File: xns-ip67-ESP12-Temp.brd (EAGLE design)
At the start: 65.3 x 137.2 mm, 76 parts, among them CN2 JSTPH, J1 DCJ0202, SW1 KMR2, SW2 KMR2, U2 MCP73831T-2ACI/OT, U3 A7, X1 ESP-12E

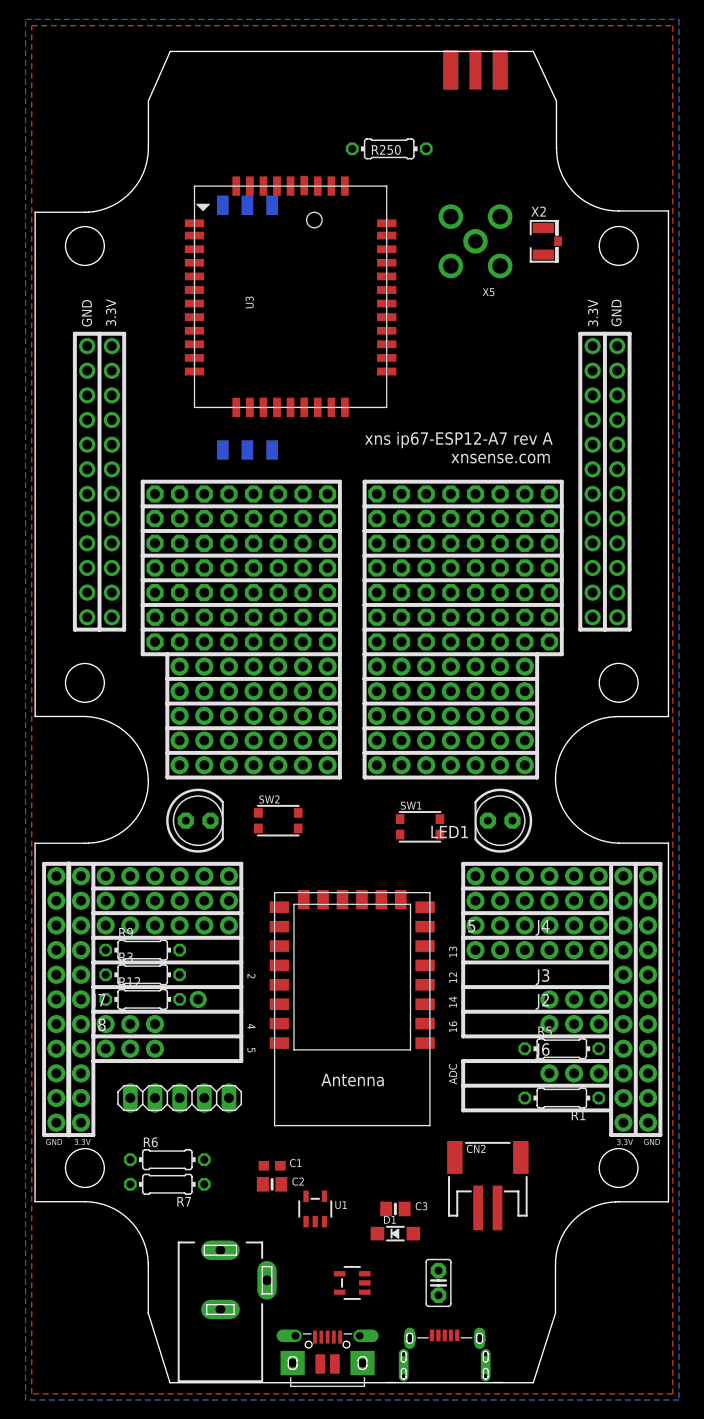
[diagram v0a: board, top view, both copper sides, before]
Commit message: New board for Temp
New board for Temp logging with A7, Power lines is routed
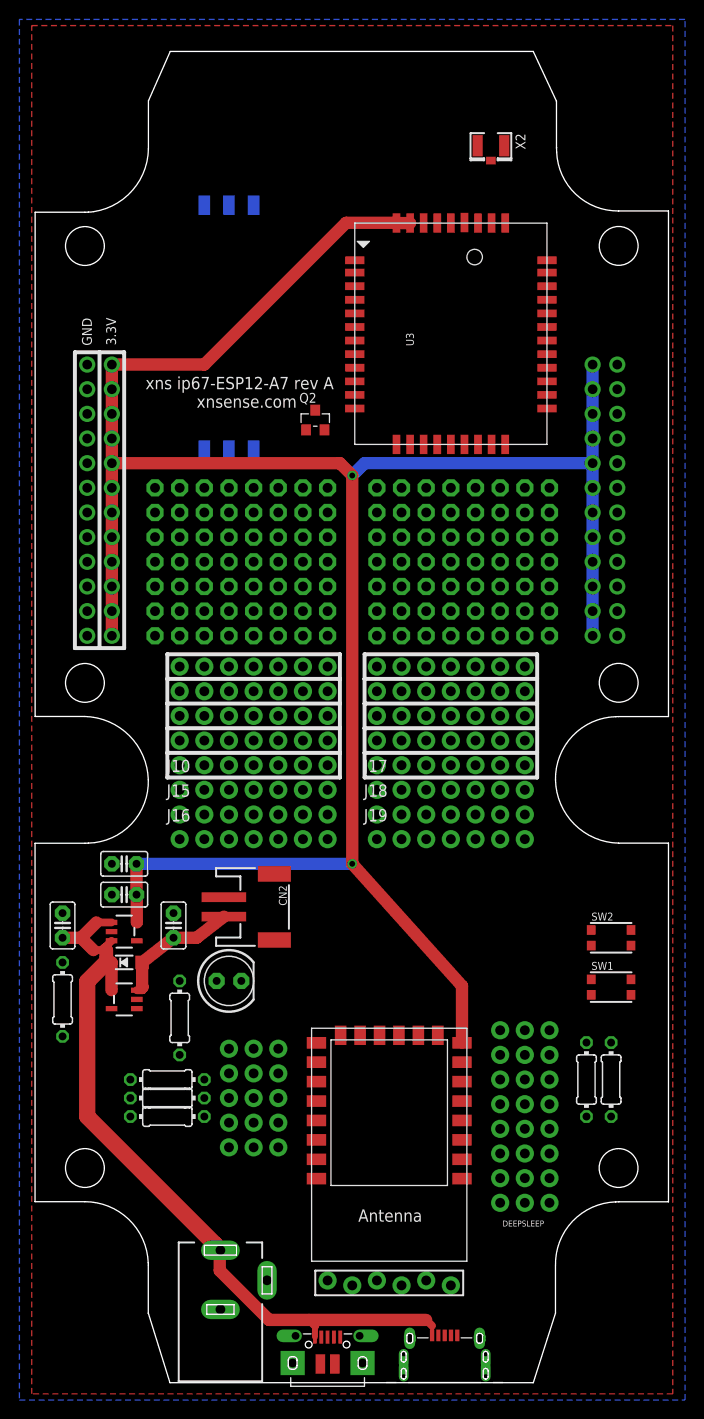
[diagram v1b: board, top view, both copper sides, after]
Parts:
- removed C1: 1uF, microbuilder:0603-NO
- removed C2, C3: 10µF, microbuilder:0805-NO
- removed J21, J22, J23: (no value), SparkFun-Connectors:1X06_NO_SILK
- removed JP3: (no value), adafruit:1X01-CLEANBIG
- removed JP37: (no value), pinhead:1X05
- removed LED1: Red, adafruit:LED5MM
- removed R250: (no value), eagle-ltspice:0204/7
- removed X3: (no value), adafruit:SMA_EDGELAUNCH
- removed X5: (no value), adafruit:SMA90_DIP
- added C5, C6: 10uF, capacitor-wima:C2.5-2
- added C7: 1uF, capacitor-wima:C2.5-2
- added DEEPSLEEP, J11, J12, J13, J9: (no value), SparkFun-Connectors:1X03_NO_SILK
- added J10: (no value), SparkFun-Connectors:1X07_NO_SILK
- added Q2: BSN20, Discrete:SOT23@1
- J14: device SparkFun-Connectors:1X11_NO_SILK -> SparkFun-Connectors:1X03_NO_SILK
- J15, J16, J17: device SparkFun-Connectors:1X11_NO_SILK -> SparkFun-Connectors:1X07_NO_SILK
- J18, J19: device SparkFun-Connectors:1X06_NO_SILK -> SparkFun-Connectors:1X07_NO_SILK
- J20: device SparkFun-Connectors:1X06_NO_SILK -> SparkFun-Connectors:1X06_FEMALE_LOCK.010
- moved J16 56.4 mm to (19.1, 57.1), turned to 0 degrees
- moved C4 45.8 mm to (18.4, 48.3), turned to 90 degrees
- moved J14 45.7 mm to (52.1, 27.3), turned to 0 degrees
- moved J20 43.3 mm to (34.3, 11.4)
- moved J17 42.7 mm to (39.4, 62.2), turned to 0 degrees
- moved D1 39.5 mm to (13.3, 44.5)
- moved U2 37.5 mm to (13.3, 40.6)
- moved J25 37.0 mm to (54.6, 64.8), turned to 180 degrees
- moved J29 37.0 mm to (54.6, 74.9), turned to 180 degrees
- moved SW2 36.4 mm to (63.5, 47.0)
- moved CN2 36.0 mm to (27.3, 50.2), turned to 270 degrees
- moved J26 35.9 mm to (54.6, 67.3), turned to 180 degrees
- moved J28 35.9 mm to (54.6, 72.4), turned to 180 degrees
- moved J27 35.6 mm to (54.6, 69.8), turned to 180 degrees
- moved U1 34.7 mm to (13.3, 47.6), turned to 270 degrees
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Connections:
- removed net N$19: J21.1, J21.2, J21.3, J21.4, J21.5, J21.6
- removed net N$20: J22.1, J22.2, J22.3, J22.4, J22.5, J22.6
- removed net N$5: LED1.K, R12.1
- removed net N$6: J7.1, J7.2, J7.3, X1.13
- removed net N$7: X5.GND3, X5.GND4
- removed net N$70: J23.1, J23.2, J23.3, J23.4, J23.5, J23.6
- removed net N$9: J8.1, J8.2, J8.3, X1.14
- removed net PWD_KEY: J2.1, J2.2, J2.3, U3.8, X1.4
- new net N$12: J10.1, J10.2, J10.3, J10.4, J10.5, J10.6, J10.7
- new net N$14: J15.1, J15.2, J15.3, J15.4, J15.5, J15.6, J15.7
- new net N$15: J16.1, J16.2, J16.3, J16.4, J16.5, J16.6, J16.7
- new net PWR_KEY: DEEPSLEEP.2, J2.1, J2.2, J2.3, X1.4
- net 3.3V: now also C6.1, C7.1, R12.1, U1.5; no longer C1.1, C2.1, J15.1, J15.10, J15.11, J15.2, J15.3, J15.4, J15.5, J15.6, J15.7, J15.8, J15.9, J17.1, J17.10, J17.11, J17.2, J17.3, J17.4, J17.5, J17.6, J17.7, J17.8, J17.9, LED1.A
- net CH_PD: now also J14.1, J14.2, J14.3
- net GND: now also C5.2, C6.2, C7.2, J20.1, Q2.2; no longer C1.2, C2.2, C3.2, J14.1, J14.10, J14.11, J14.2, J14.3, J14.4, J14.5, J14.6, J14.7, J14.8, J14.9, J16.1, J16.10, J16.11, J16.2, J16.3, J16.4, J16.5, J16.6, J16.7, J16.8, J16.9, JP37.1, X3.GND@1, X3.GND@2, X3.GND@3, X3.GND@4
- net GPIO0: now also J9.1, J9.2, J9.3, Q2.1; no longer JP3.1
- net GPIO15: now also J12.1, J12.2, J12.3, U3.8
- net GPIO2: now also J13.1, J13.2, J13.3
- net N$1: now also J3.1, J3.2, J3.3, X1.5; no longer R250.1, U3.35
- net N$16: now also J17.1, J17.2, J17.3, J17.4, J17.5, J17.6, J17.7; no longer J18.1, J18.2, J18.3, J18.4, J18.5, J18.6
- net N$17: now also J18.1, J18.2, J18.3, J18.4, J18.5, J18.6, J18.7; no longer J19.1, J19.2, J19.3, J19.4, J19.5, J19.6
- net N$18: now also J19.1, J19.2, J19.3, J19.4, J19.5, J19.6, J19.7; no longer J20.1, J20.2, J20.3, J20.4, J20.5, J20.6
- net N$3: now also U3.35; no longer R250.2, X3.P, X5.ANTENNA
- net N$4: now also J5.1, J5.2, J5.3, X1.7; no longer X5.GND1, X5.GND2
- net RESET: now also DEEPSLEEP.3, J11.1, J11.2, J11.3
- net RESET_KEY: now also Q2.3
- net RX: now also J20.4; no longer JP37.4
- net TX: now also J20.5; no longer JP37.5
- net UART_RX: now also J7.1, J7.2, J7.3, X1.13; no longer J5.1, J5.2, J5.3, X1.7
- net UART_TX: now also J8.1, J8.2, J8.3, X1.14; no longer J3.1, J3.2, J3.3, X1.5
- net VCC: now also C5.1; no longer C3.1
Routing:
- net 3.3V: track 0.00 -> 234.4 mm, vias 0 -> 2
- net VCC: track 0.00 -> 80.2 mm
- net V_BATT: track 0.00 -> 13.6 mm
- added copper zone on layer 16, net N$19
- removed copper zone on layer 16, net N$11
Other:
- board text removed: "12"
- board text removed: "13"
- board text removed: "14"
- board text removed: "16"
- board text removed: "2"
- board text removed: "4"
- board text removed: "5"
- board text removed: "ADC"
- board text removed: "RX"
- board text removed: "TX"

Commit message: Eagle Upgrade, Routing finished alpha
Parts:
- removed JCB_MICROUSB: (no value), jcbrataas-2:USB-MICRO-B
- removed JP10, JP11, JP12, JP13, JP14, JP15, JP25, JP26, JP27, JP28, JP29, JP30, JP35, JP36: (no value), adafruit:1X08-CLEANBIG
- removed SW1, SW2: KMR2, microbuilder:BTN_KMR2_4.6X2.8
- added 5V: (no value), SparkFun-Connectors:1X01NS-KIT
- added DATAEXCHANGE: (no value), SparkFun-Connectors:1X06_FEMALE_LOCK.010
- added J21, J22, J23, J24, J35, J36, J37, J38, J39, J40, J41, J42, J43: (no value), SparkFun-Connectors:1X08_NO_SILK
- added PROG, RESET: KMR2, microbuilder:BTN_KMR2_4.6X2.8
- J11, J12, J13, J14, J2, J3, J4, J5, J6, J7, J8, J9: device SparkFun-Connectors:1X03_NO_SILK -> SparkFun-Connectors:1X01NS-KIT
- J20: device SparkFun-Connectors:1X06_FEMALE_LOCK.010 -> SparkFun-Connectors:1X08_NO_SILK
- U2: value MCP73831T-2ACI/OT -> MCP73831
- moved J20 77.0 mm to (16.5, 86.4)
- moved J7 28.3 mm to (51.4, 20.3)
- moved J12 27.8 mm to (51.4, 30.5)
- moved J9 27.8 mm to (51.4, 25.4)
- moved J8 27.4 mm to (51.4, 22.9)
- moved J13 27.3 mm to (51.4, 33.0)
- moved J6 24.2 mm to (29.8, 34.3)
- moved J2 23.9 mm to (29.8, 21.0)
- moved J3 23.9 mm to (29.8, 23.5)
- moved J5 22.9 mm to (29.8, 31.8)
- moved J4 22.9 mm to (29.8, 29.2)
- moved R7 16.3 mm to (22.9, 36.8), turned to 0 degrees
- moved DEEPSLEEP 11.7 mm to (64.8, 28.6)
- moved J14 8.28 mm to (51.4, 35.6)
- moved Q2 7.96 mm to (29.2, 107.3)
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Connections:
- net N$22 renamed SIM_DATA
- net N$23 renamed VSIM
- removed net N$30: JP10.1, JP10.2, JP10.3, JP10.4, JP10.5, JP10.6, JP10.7, JP10.8
- removed net N$31: JP11.1, JP11.2, JP11.3, JP11.4, JP11.5, JP11.6, JP11.7, JP11.8
- removed net N$32: JP12.1, JP12.2, JP12.3, JP12.4, JP12.5, JP12.6, JP12.7, JP12.8
- removed net N$33: JP13.1, JP13.2, JP13.3, JP13.4, JP13.5, JP13.6, JP13.7, JP13.8
- removed net N$34: JP14.1, JP14.2, JP14.3, JP14.4, JP14.5, JP14.6, JP14.7, JP14.8
- removed net N$35: JP15.1, JP15.2, JP15.3, JP15.4, JP15.5, JP15.6, JP15.7, JP15.8
- removed net N$36: JP30.1, JP30.2, JP30.3, JP30.4, JP30.5, JP30.6, JP30.7, JP30.8
- removed net N$37: JP29.1, JP29.2, JP29.3, JP29.4, JP29.5, JP29.6, JP29.7, JP29.8
- removed net N$38: JP28.1, JP28.2, JP28.3, JP28.4, JP28.5, JP28.6, JP28.7, JP28.8
- removed net N$39: JP27.1, JP27.2, JP27.3, JP27.4, JP27.5, JP27.6, JP27.7, JP27.8
- removed net N$40: JP26.1, JP26.2, JP26.3, JP26.4, JP26.5, JP26.6, JP26.7, JP26.8
- removed net N$41: JP25.1, JP25.2, JP25.3, JP25.4, JP25.5, JP25.6, JP25.7, JP25.8
- removed net N$50: JP35.1, JP35.2, JP35.3, JP35.4, JP35.5, JP35.6, JP35.7, JP35.8
- removed net N$51: JP36.1, JP36.2, JP36.3, JP36.4, JP36.5, JP36.6, JP36.7, JP36.8
- removed net PWR_KEY: DEEPSLEEP.2, J2.1, J2.2, J2.3, X1.4
- new net ADC: J8.1, X1.2
- new net GPIO12: J13.1, X1.6
- new net GPIO13: J14.1, X1.7
- new net GPIO14: J12.1, X1.5
- new net GPIO16: DEEPSLEEP.2, J11.1, X1.4
- new net N$11: J40.1, J40.2, J40.3, J40.4, J40.5, J40.6, J40.7, J40.8
- new net N$19: J42.1, J42.2, J42.3, J42.4, J42.5, J42.6, J42.7, J42.8
- new net N$20: J36.1, J36.2, J36.3, J36.4, J36.5, J36.6, J36.7, J36.8
- new net N$21: J43.1, J43.2, J43.3, J43.4, J43.5, J43.6, J43.7, J43.8
- new net N$5: J23.1, J23.2, J23.3, J23.4, J23.5, J23.6, J23.7, J23.8
- new net N$6: J24.1, J24.2, J24.3, J24.4, J24.5, J24.6, J24.7, J24.8
- new net N$7: J35.1, J35.2, J35.3, J35.4, J35.5, J35.6, J35.7, J35.8
- new net N$9: J38.1, J38.2, J38.3, J38.4, J38.5, J38.6, J38.7, J38.8
- new net SIM_CLK: SIMCARD.C2, U3.15
- new net SIM_RST: SIMCARD.C3, U3.14
- net CH_PD: now also J9.1; no longer J14.1, J14.2, J14.3
- net GND: now also DATAEXCHANGE.1, PROG.A, PROG.A', RESET.A, RESET.A'; no longer J20.1, JCB_MICROUSB.BL1, JCB_MICROUSB.BL2, JCB_MICROUSB.BL3, JCB_MICROUSB.BL4, JCB_MICROUSB.BR1, JCB_MICROUSB.BR2, JCB_MICROUSB.BR3, JCB_MICROUSB.BR4, JCB_MICROUSB.GND, JCB_MICROUSB.MTL1, JCB_MICROUSB.MTL2, JCB_MICROUSB.MTR1, JCB_MICROUSB.MTR2, SW1.A, SW1.A', SW2.A, SW2.A'
- net GPIO0: now also J4.1, PROG.B, PROG.B'; no longer J9.1, J9.2, J9.3, SW2.B, SW2.B'
- net GPIO15: now also J6.1; no longer J12.1, J12.2, J12.3
- net GPIO2: now also J5.1; no longer J13.1, J13.2, J13.3
- net N$1: now also J20.1, J20.2, J20.3, J20.4, J20.5, J20.6, J20.7, J20.8; no longer J3.1, J3.2, J3.3, X1.5
- net N$10: now also J39.1, J39.2, J39.3, J39.4, J39.5, J39.6, J39.7, J39.8; no longer SIMCARD.C2, U3.14
- net N$13: now also J41.1, J41.2, J41.3, J41.4, J41.5, J41.6, J41.7, J41.8; no longer SIMCARD.C3, U3.15
- net N$2: now also J21.1, J21.2, J21.3, J21.4, J21.5, J21.6, J21.7, J21.8; no longer J4.1, J4.2, J4.3, X1.6
- net N$4: now also J22.1, J22.2, J22.3, J22.4, J22.5, J22.6, J22.7, J22.8; no longer J5.1, J5.2, J5.3, X1.7
- net N$8: now also J37.1, J37.2, J37.3, J37.4, J37.5, J37.6, J37.7, J37.8; no longer J6.1, J6.2, J6.3, X1.2
- net RESET: now also J7.1, RESET.B, RESET.B'; no longer J11.1, J11.2, J11.3, SW1.B, SW1.B'
- net RX: now also DATAEXCHANGE.4, J3.1; no longer J20.4
- net TX: now also DATAEXCHANGE.5, J2.1; no longer J20.5
- net UART_RX: no longer J7.1, J7.2, J7.3
- net UART_TX: no longer J8.1, J8.2, J8.3
- net VCC: now also 5V.1; no longer JCB_MICROUSB.VBUS
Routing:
- net GPIO0: track 0.00 -> 151.2 mm, vias 0 -> 4
- net GPIO15: track 0.00 -> 127.5 mm, vias 0 -> 4
- net UART_TX: track 0.00 -> 106.8 mm, vias 0 -> 2
- net UART_RX: track 0.00 -> 101.1 mm, vias 0 -> 2
- net 3.3V: track 234.4 -> 289.1 mm, vias 2 -> 4
- net RESET: track 0.00 -> 38.1 mm
- net SIM_DATA: track 0.00 -> 38.0 mm, vias 0 -> 1
- net VSIM: track 0.00 -> 35.8 mm, vias 0 -> 1
- net RX: track 0.00 -> 30.6 mm
- net SIM_CLK: track 0.00 -> 28.7 mm, vias 0 -> 1
- net TX: track 0.00 -> 25.2 mm
- net VCC: track 80.2 -> 104.6 mm
- net CH_PD: track 0.00 -> 22.2 mm
- net SIM_RST: track 0.00 -> 19.5 mm, vias 0 -> 1
- net N$52: track 0.00 -> 16.7 mm
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- added copper zone on layer 16, net GND
- removed copper zone on layer 16, net N$19
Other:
- board text added: "0"
- board text added: "12"
- board text added: "13"
- board text added: "14"
- board text added: "15"
- board text added: "16"
- board text added: "2"
- board text added: "5V"
- board text added: "ADC"
- board text added: "CHP"
- board text added: "RST"
- board text added: "RX"
- board text added: "TX"

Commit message: Cleanup, add PIN's
Added Pin for GPIO’s
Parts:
- added J44, J45: (no value), SparkFun-Connectors:1X01NS-KIT
- moved R6 2.54 mm to (22.9, 36.8)
- moved R7 2.54 mm to (22.9, 34.3)
- moved J2 1.27 mm to (29.8, 19.7)
- moved J3 1.27 mm to (29.8, 22.2)
- moved J4 0.63 mm to (29.8, 29.8)
- moved J5 0.63 mm to (29.8, 32.4)
- moved J6 0.63 mm to (29.8, 34.9)
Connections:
- net UART_RX: now also J45.1
- net UART_TX: now also J44.1
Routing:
- net N$59: track 9.72 -> 5.08 mm
- net UART_TX: track 106.8 -> 110.7 mm
- net UART_RX: track 101.1 -> 104.7 mm
- net N$55: track 11.9 -> 9.78 mm
- net TX: track 25.2 -> 24.3 mm
- net N$24: track 8.20 -> 8.91 mm
- net RX: track 30.6 -> 29.9 mm
- net 3.3V: track 289.1 -> 289.6 mm
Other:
- board text added: "3.3v"
- board text added: "4"
- board text added: "5"
- board text added: "AI THINKER"
